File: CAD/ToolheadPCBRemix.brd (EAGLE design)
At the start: 44.8 x 33.3 mm, 18 parts

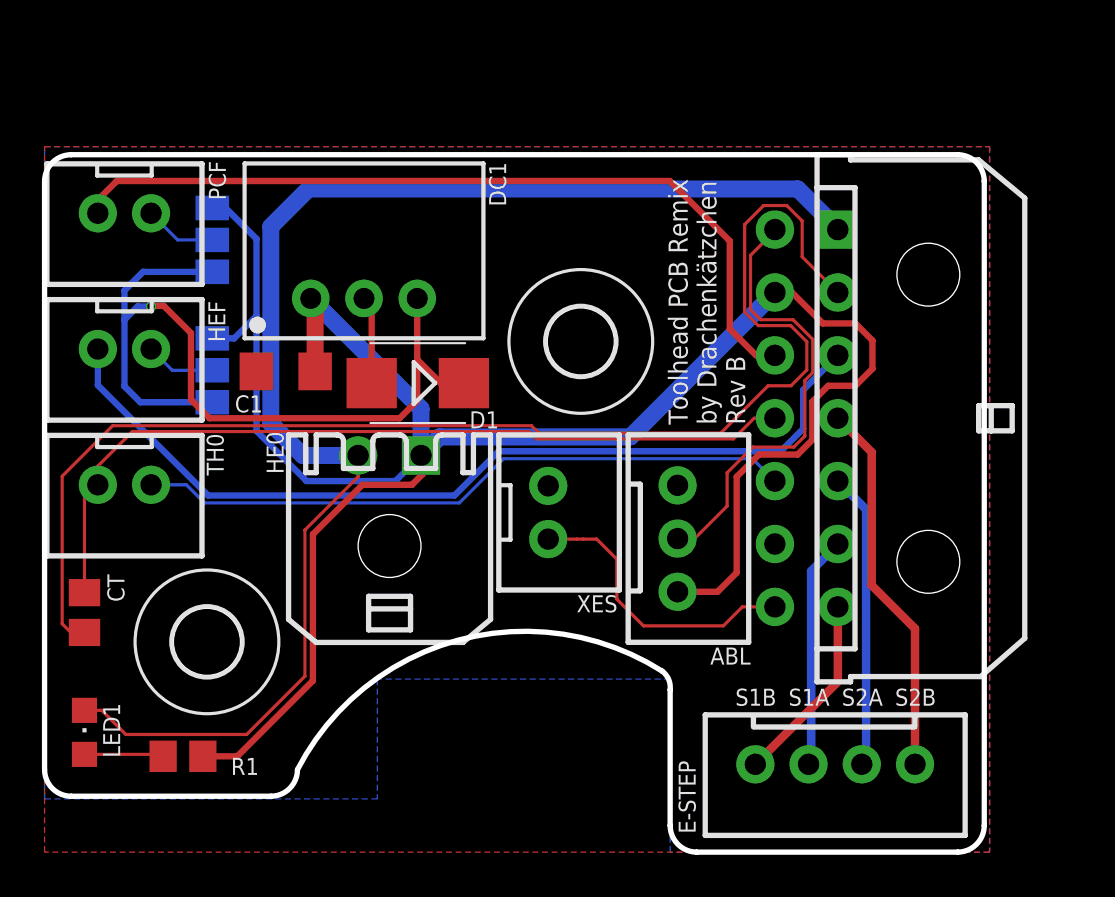
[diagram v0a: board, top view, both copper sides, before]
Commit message: Update to dual vregs (12V/5V)
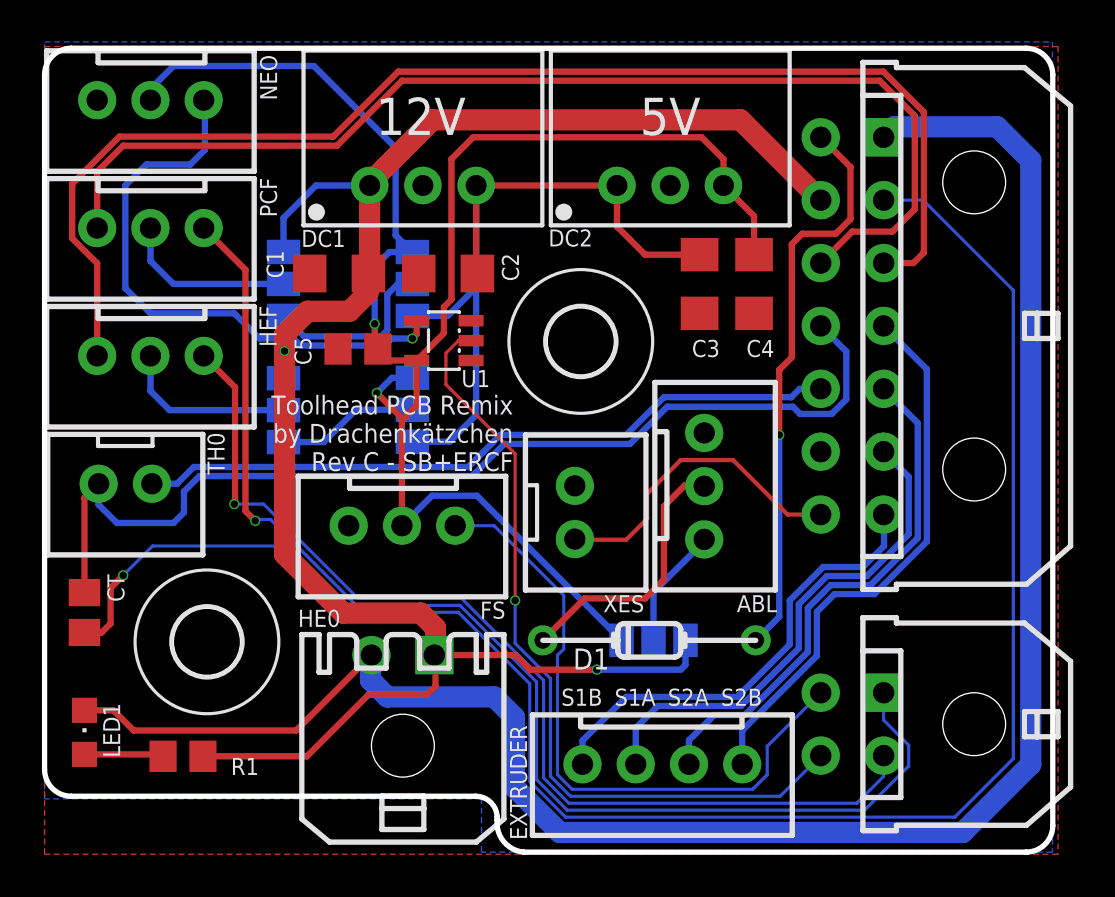
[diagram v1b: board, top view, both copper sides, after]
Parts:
- removed E-STEP: JST-XH-04-PIN-ROUND-PAD, Rembrandt Electronics - JST XH Connectors v1-0:JST-XH-04-PACKAGE-ROUND-PAD
- added C2: 22µ 25V, rcl:C1206
- added C3, C4: 10µ 50V, rcl:C1206
- added C5: 100n, rcl:C0805
- added DC2: R-78E5.0-0.5, dc-dc-converter:SIP3
- added EXTRUDER: JST-XH-04-PIN-ROUND-PAD, Rembrandt Electronics - JST XH Connectors v1-0:JST-XH-04-PACKAGE-ROUND-PAD
- added FS, NEO: JST-XH-03-PIN-ROUND-PAD, Rembrandt Electronics - JST XH Connectors v1-0:JST-XH-03-PACKAGE-ROUND-PAD
- added MCU-EXT: (no value), con-molex-micro-fit-3_0:43045-0400
- added SJ3, SJ4, SJ5: (no value), jumper:SJ_2
- added U1: 74LVC1G17, logick:SOT23-5
- C1: value (none) -> 10µ 50V
- D1: value 1SMB5928BT3G -> BAT85; device diode:SMB -> nxp_60_1_1:SOD68
- HEF, PCF: value JST-XH-02-PIN-ROUND-PAD -> JST-XH-03-PIN-ROUND-PAD; device Rembrandt Electronics - JST XH Connectors v1-0:JST-XH-02-PACKAGE-ROUND-PAD -> Rembrandt Electronics - JST XH Connectors v1-0:JST-XH-03-PACKAGE-ROUND-PAD
- moved D1 16.5 mm to (86.0, 59.0)
- moved HE0 9.55 mm to (74.2, 54.0)
- moved DC1 6.08 mm to (75.2, 80.7)
- moved C1 5.32 mm to (71.2, 76.5)
- moved MCU 4.92 mm to (101.5, 74.0)
- moved SJ2 4.00 mm to (68.6, 76.0)
- moved SJ1 3.89 mm to (68.6, 70.0)
- moved ABL 2.80 mm to (89.9, 66.4)
- moved PCF 1.43 mm to (62.2, 77.4)
- moved HEF 1.28 mm to (62.2, 71.3)
- moved XES 1.27 mm to (83.7, 65.1)
- moved TH0 0.06 mm to (61.0, 65.2)
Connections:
- new net 5V: C4.2, C5.2, DC2.3, FS.2, NEO.2, SJ3.1, SJ4.1, SJ5.1, U1.5
- new net DIN: MCU-EXT.P$4, U1.2
- new net FS: FS.3, MCU-EXT.P$3
- new net HEF-TACH: HEF.3, MCU-EXT.P$2
- new net N$10: ABL.2, D1.C
- new net N$4: NEO.3, U1.4
- new net N$5: SJ2.1, SJ3.2
- new net N$8: SJ1.1, SJ4.2
- new net N$9: ABL.1, SJ5.2
- new net PCF-TACH: MCU-EXT.P$1, PCF.3
- net 12V: now also C2.2, C3.2, DC2.1, SJ3.3, SJ4.3; no longer D1.C, SJ1.1, SJ2.1
- net 24V: now also SJ5.3; no longer ABL.1
- net ABL: now also D1.A; no longer ABL.2
- net GND: now also C2.1, C3.1, C4.1, C5.1, DC2.2, FS.1, NEO.1, U1.3; no longer D1.A
- net S1A: now also EXTRUDER.2; no longer E-STEP.2
- net S1B: now also EXTRUDER.1; no longer E-STEP.1
- net S2A: now also EXTRUDER.3; no longer E-STEP.3
- net S2B: now also EXTRUDER.4; no longer E-STEP.4
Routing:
- net 5V: track 0.00 -> 83.0 mm, vias 0 -> 2
- net PCF-TACH: track 0.00 -> 59.5 mm, vias 0 -> 1
- net HEF-TACH: track 0.00 -> 48.9 mm, vias 0 -> 1
- net DIN: track 0.00 -> 37.8 mm, vias 0 -> 1
- net FS: track 0.00 -> 30.8 mm
- net N$4: track 0.00 -> 27.7 mm, vias 0 -> 1
- net HE0: track 66.5 -> 91.3 mm
- net CT: track 62.8 -> 86.6 mm, vias 0 -> 1
- net HEF: track 43.1 -> 61.2 mm
- net PCF: track 39.2 -> 54.2 mm
- net S1A: track 11.1 -> 24.2 mm
- net S1B: track 9.14 -> 22.1 mm
- net N$10: track 0.00 -> 12.8 mm
- net 24V: track 102.6 -> 90.2 mm, vias 0 -> 2
- net S2A: track 14.2 -> 25.1 mm
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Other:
- board size 44.8 x 33.3 mm -> 48.1 x 38.4 mm
- board text added: "+"
- board text added: "-"
- board text added: "12V"
- board text added: "24V"
- board text added: "5V"
- board text added: "ABL"
- board text added: "AGND"
- board text added: "CT"
- board text added: "DATA"
- board text added: "DIN"
- board text added: "FS"
- board text added: "GND"
- board text added: "HEF"
- board text added: "JLCJLCJLCJLC"
- board text added: "PC"
- board text added: "PCF"
- board text added: "SIG"
- board text added: "TACHO"
- board text added: "TH0"
- board text added: "Toolhead PCB Remix by Drachenkätzchen Rev C - SB+ERCF"
- board text added: "VCC"
- board text added: "XES"
- board text removed: "24V HEF 12V"
- board text removed: "24V PCB 12V"
- board text removed: "Toolhead PCB Remix by Drachenkätzchen Rev B"
